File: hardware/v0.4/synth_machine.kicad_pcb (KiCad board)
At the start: 2 copper layers, 160 x 74 mm, 123 parts, among them J1 USB-C (MIDI + 5V power), J10 Pot VOL (10k lin, panel) JST-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, J15 STEMMA QT (I2C1), J16 Power switch (panel SPST) JST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, J17 Battery 1S LiPo (JST-PH, 1 = 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, J5 Speaker L (JST-PH), J6 Speaker R (JST-PH), J7 Headphones 3.5mm (CUI SJ1-351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, J8 Expansion, J9 Display (SPI1), K1 KEY C4 (direct D10) JST-XH, K10 A4 [c2 r2] JST-XH, K11 A#4 [c1 r1] JST-XH, K12 B4 [c1 r2] JST-XH, K13 C5 [c0 r2] JST-XH, K14 BTN1 [c0 r0] JST-XH, K15 BTN2 [c0 r1] JST-XH, K16 BTN3 [c1 r0] JST-XH, K17 BTN4 [c2 r0] JST-XH, K18 BTN5 [c3 r0] JST-XH, K19 BTN6 [c4 r0] JST-XH, K2 C#4 [c5 r0] JST-XH, K3 D4 [c5 r1] JST-XH, K4 D#4 [c4 r1] JST-XH, K5 E4 [c5 r2] JST-XH, K6 F4 [c4 r2] JST-XH, K7 F#4 [c3 r1] JST-XH, K8 G4 [c3 r2] JST-XH, K9 G#4 [c2 r1] JST-XH, Q1 2N7002, Q2 2N7002, U1 Daisy Seed / Seed3, U2 TPA6138A2PWR, U3 MAX98306ETD+T, U4 USBLC6-2SC6, U5 BQ24074RGTR, U6 TPS61023DRLR, U7 AP7361C-33E-13

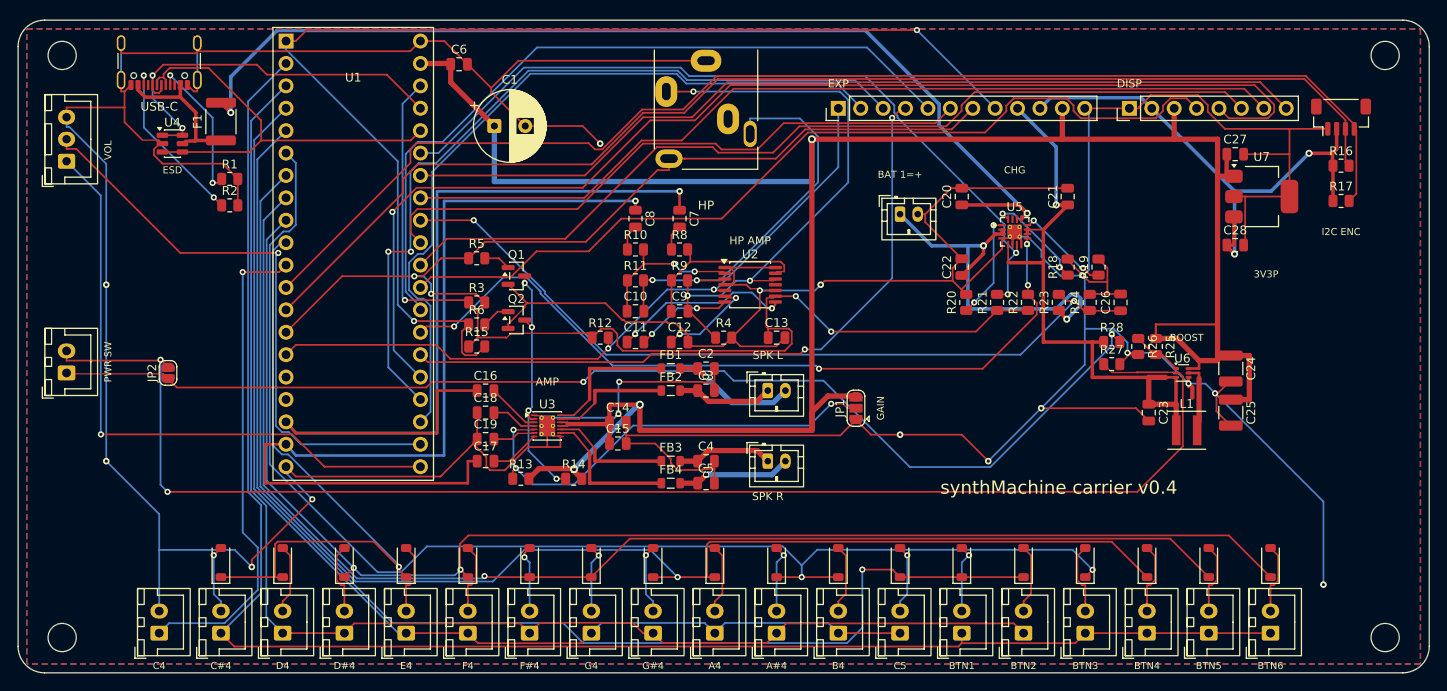
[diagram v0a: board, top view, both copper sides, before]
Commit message: Carrier v0.4: 1.5 mm between U7 and its capacitors
C27 was 0.13 mm from the regulator's courtyard and C28 0.84 mm; U7 moved
1.5 mm down and C28 2 mm down. DRC 0 unconnected, ERC clean.

Co-Authored-By: Claude Fable 5.1 <noreply@anthropic.com>
Claude-Session: https://claude.ai/code/session_019ZDGV5fm4G7LwUwRWHEiwx
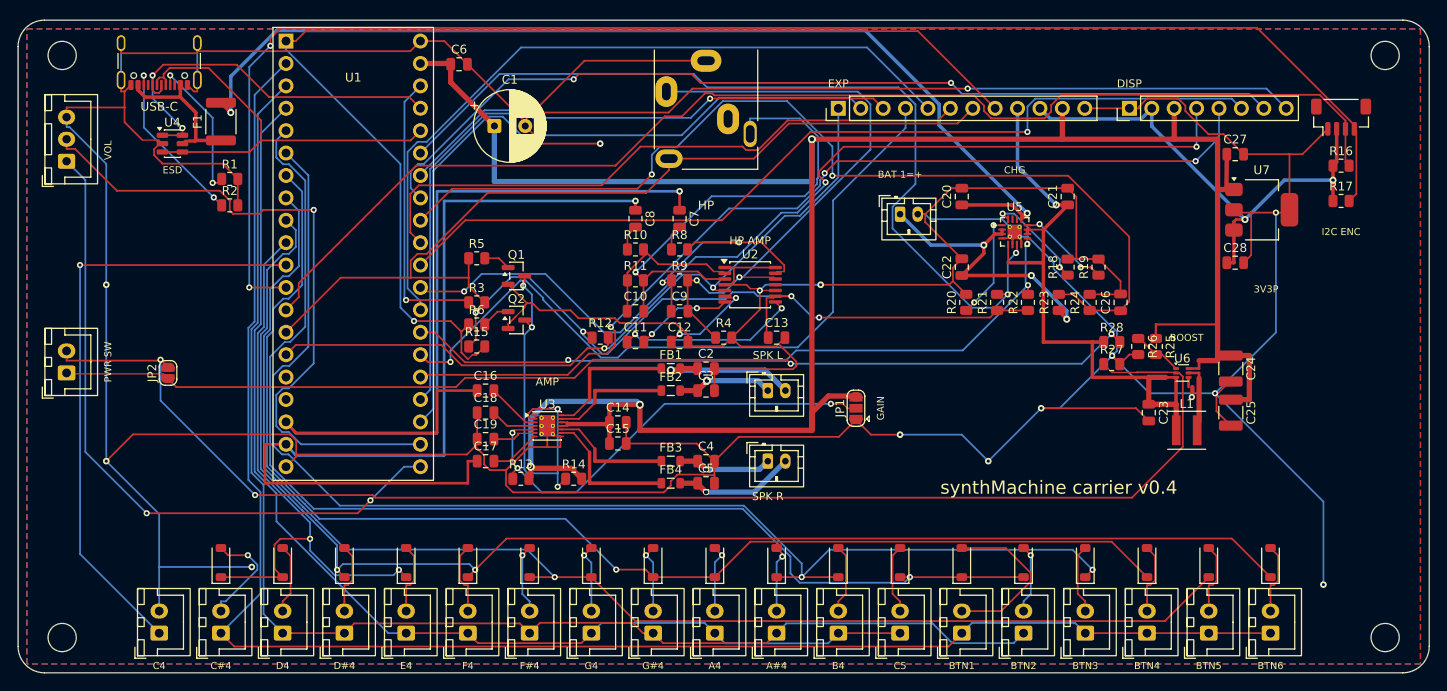
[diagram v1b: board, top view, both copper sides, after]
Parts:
- moved C28 2.00 mm to (138.0, 27.5)
- moved U7 1.50 mm to (141.0, 21.5)
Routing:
- net SPI_MOSI: track 134.7 -> 107.6 mm, vias 1 -> 3
- net I2C_SCL: track 144.0 -> 170.4 mm, vias 0 -> 2
- net VBAT_SENSE: track 90.9 -> 112.1 mm
- net GND: track 680.7 -> 699.2 mm, vias 17 -> 14
- net AMP_SD: track 28.5 -> 42.7 mm
- net KEY_C4: track 55.2 -> 68.8 mm
- net USB_PGOOD: track 89.3 -> 101.1 mm
- net KBTN1_D: track 7.83 -> 19.2 mm, vias 1 -> 0
- net POT_VOL: track 67.0 -> 76.9 mm
- net SW_HI: track 132.8 -> 123.4 mm
- net COL2: track 153.4 -> 144.1 mm
- net VBAT: track 43.4 -> 34.4 mm, vias 2 -> 3
- net HP_INL: track 20.6 -> 29.4 mm, vias 0 -> 2
- net HP_R: track 46.7 -> 55.2 mm, vias 2 -> 1
- net COL0: track 143.7 -> 135.6 mm
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
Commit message: Carrier v0.4: USB-C receptacle is the HRO TYPE-C-31-M-12 (in stock at JLCPCB)
The GCT USB4105-GF-A went out of stock at LCSC. The HRO part has the
same shell holes and pad pitch (pad row 0.36 mm further in) and the same
body depth, so J1 keeps its place on the top edge; KiCad's footprint for
it is used, so the pads match the part exactly. LCSC C165948, a JLCPCB
basic part. F1 moved 1.5 mm to clear the slightly larger courtyard.
Re-routed: DRC 0 unconnected, ERC clean. Gerbers, BOM and CPL regenerated.

Co-Authored-By: Claude Fable 5.1 <noreply@anthropic.com>
Claude-Session: https://claude.ai/code/session_019ZDGV5fm4G7LwUwRWHEiwx
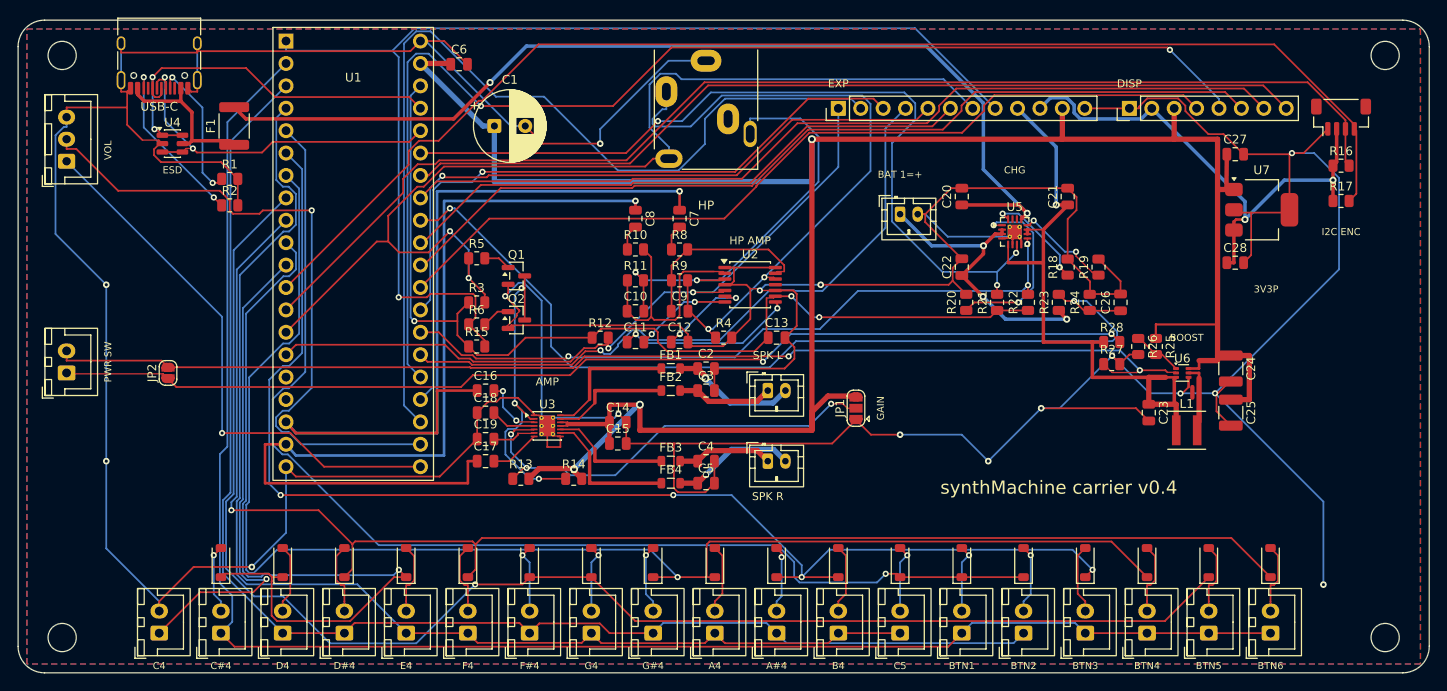
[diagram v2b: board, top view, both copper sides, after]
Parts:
- J1: footprint USB_C_Receptacle_GCT_USB4105-xx-A_16P_TopMnt_Horizontal -> USB_C_Receptacle_HRO_TYPE-C-31-M-12
- moved F1 1.58 mm to (24.5, 12.0)
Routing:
- net SPI_MOSI: track 107.6 -> 137.4 mm, vias 3 -> 2
- net EXP_A1: track 83.2 -> 108.1 mm
- net BOOST_EN: track 158.0 -> 133.7 mm
- net I2C_SCL: track 170.4 -> 146.3 mm, vias 2 -> 0
- net COL5: track 66.7 -> 89.5 mm, vias 2 -> 1
- net HP_DET: track 102.6 -> 121.8 mm, vias 0 -> 2
- net COL2: track 144.1 -> 162.1 mm
- net +3.3VA: track 76.9 -> 62.2 mm, vias 2 -> 1
- net COL3: track 152.5 -> 167.0 mm
- net KEY_C4: track 68.8 -> 55.2 mm
- net KBTN1_D: track 19.2 -> 7.83 mm, vias 0 -> 1
- net EXP_A6: track 85.3 -> 74.6 mm, vias 0 -> 1
- net HP_INR: track 17.9 -> 28.3 mm
- net ROW2: track 128.1 -> 138.5 mm
- net TS: track 11.9 -> 21.0 mm
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
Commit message: Carrier v0.4: JST headers and sockets placed by JLCPCB standard assembly
LCSC numbers on the 19 key headers, the volume and switch headers (JST XH
C158012 / C144394) and the speaker and battery sockets (JST PH C131337);
the JLCPCB placement export now includes through-hole parts. README and
Digi-Key list say which parts remain hand-fitted.

Co-Authored-By: Claude Fable 5.1 <noreply@anthropic.com>
Claude-Session: https://claude.ai/code/session_019ZDGV5fm4G7LwUwRWHEiwx
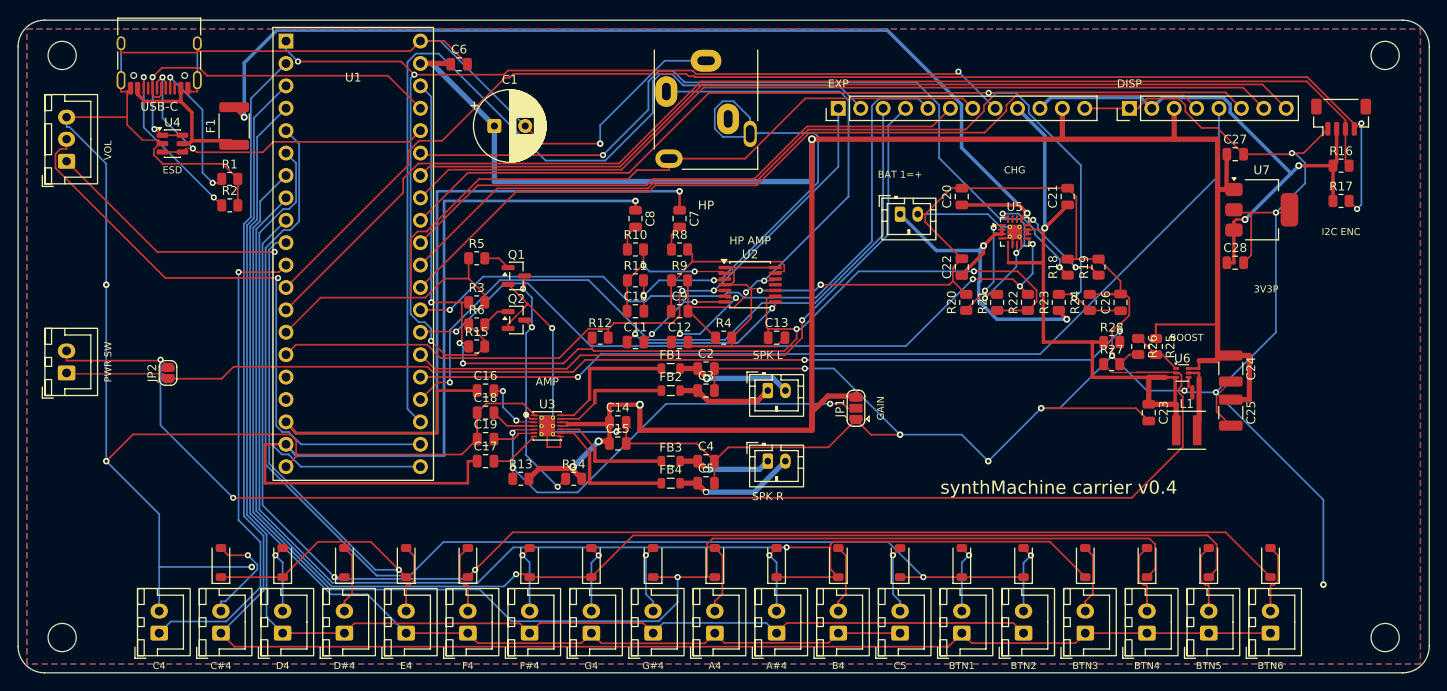
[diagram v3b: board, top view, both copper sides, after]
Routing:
- net SPI_MOSI: track 137.4 -> 107.6 mm, vias 2 -> 1
- net BOOST_EN: track 133.7 -> 159.9 mm
- net GND: track 696.8 -> 674.7 mm, vias 16 -> 18
- net COL5: track 89.5 -> 70.5 mm
- net HP_DET: track 121.8 -> 107.2 mm, vias 2 -> 0
- net +3V3: track 111.8 -> 125.0 mm, vias 3 -> 5
- net HP_INR: track 28.3 -> 17.4 mm, vias 0 -> 2
- net COL3: track 167.0 -> 156.5 mm
- net TS: track 21.0 -> 11.7 mm
- net HP_L: track 74.0 -> 64.8 mm
- net ROW2: track 138.5 -> 129.8 mm
- net POT_VOL: track 76.5 -> 68.7 mm
- net COL4: track 165.4 -> 157.7 mm, vias 1 -> 2
- net HP_R: track 49.2 -> 56.7 mm
- net AMP_SD: track 37.0 -> 29.7 mm, vias 3 -> 4
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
